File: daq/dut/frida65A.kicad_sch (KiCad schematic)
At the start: 65 parts, among them J1 SMA Molex 733910070, J2 SMA Molex 733910070, J3 RJ45 Molex 446200002, J4 DisplayPort Molex 472720024, J5 MiniFitJr Molex 469990014, J6 Conn_02x06_Top_Bottom, U1 ASIC FRIDA 65A, U2 LevelShifter TI TXV0106Q1, U3 DiffAmp TI THS4541

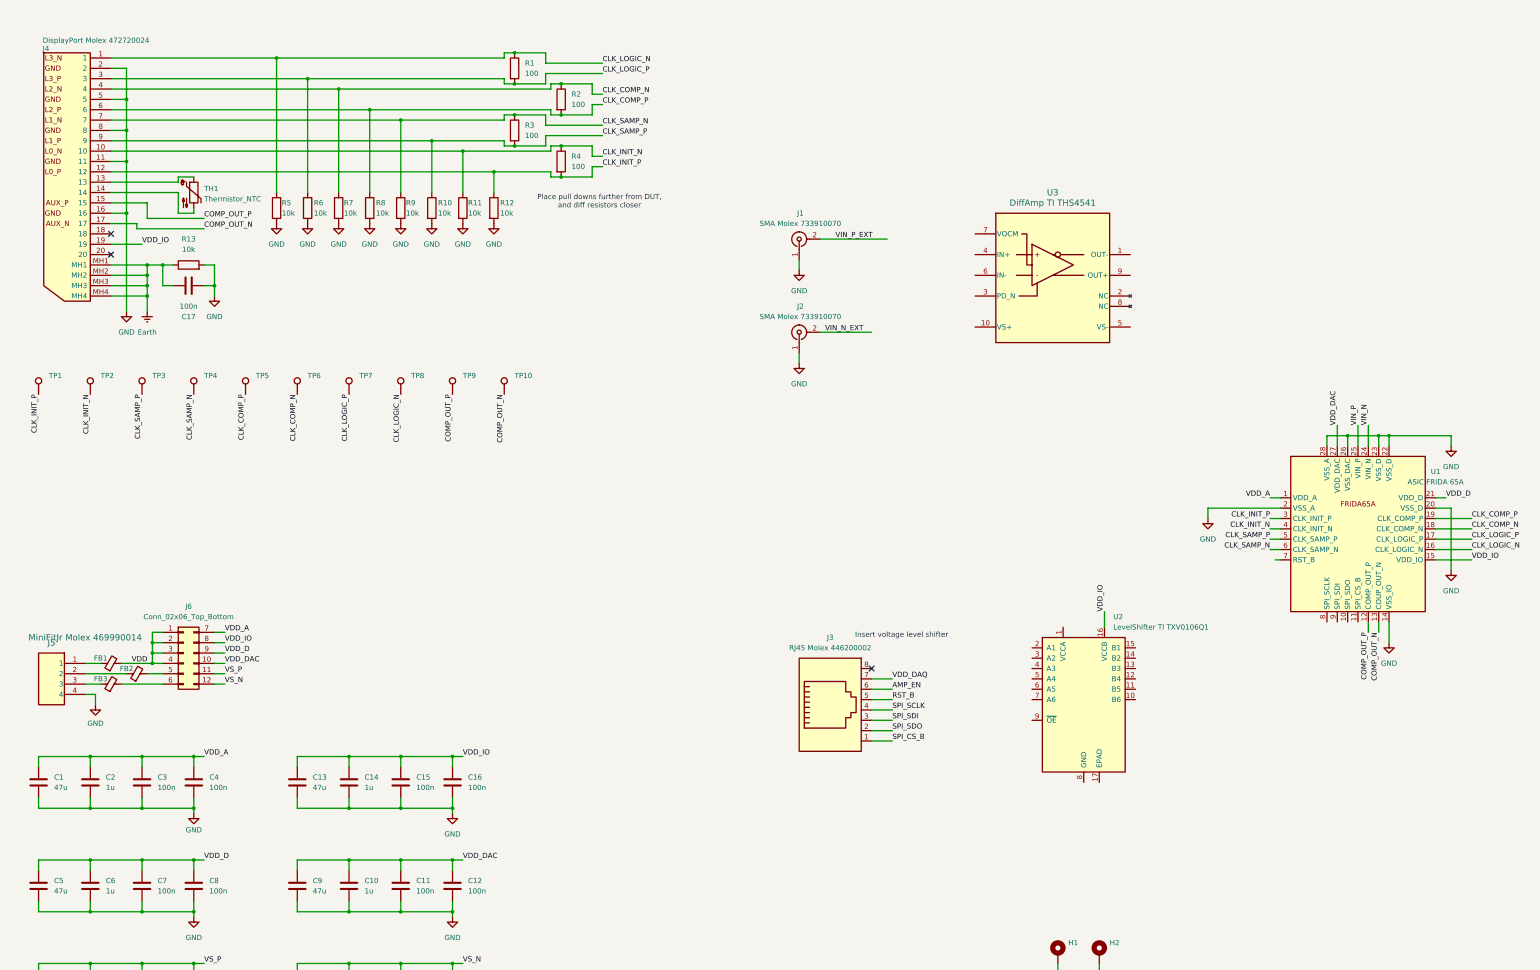
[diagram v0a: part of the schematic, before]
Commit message: Add connections for level shifter
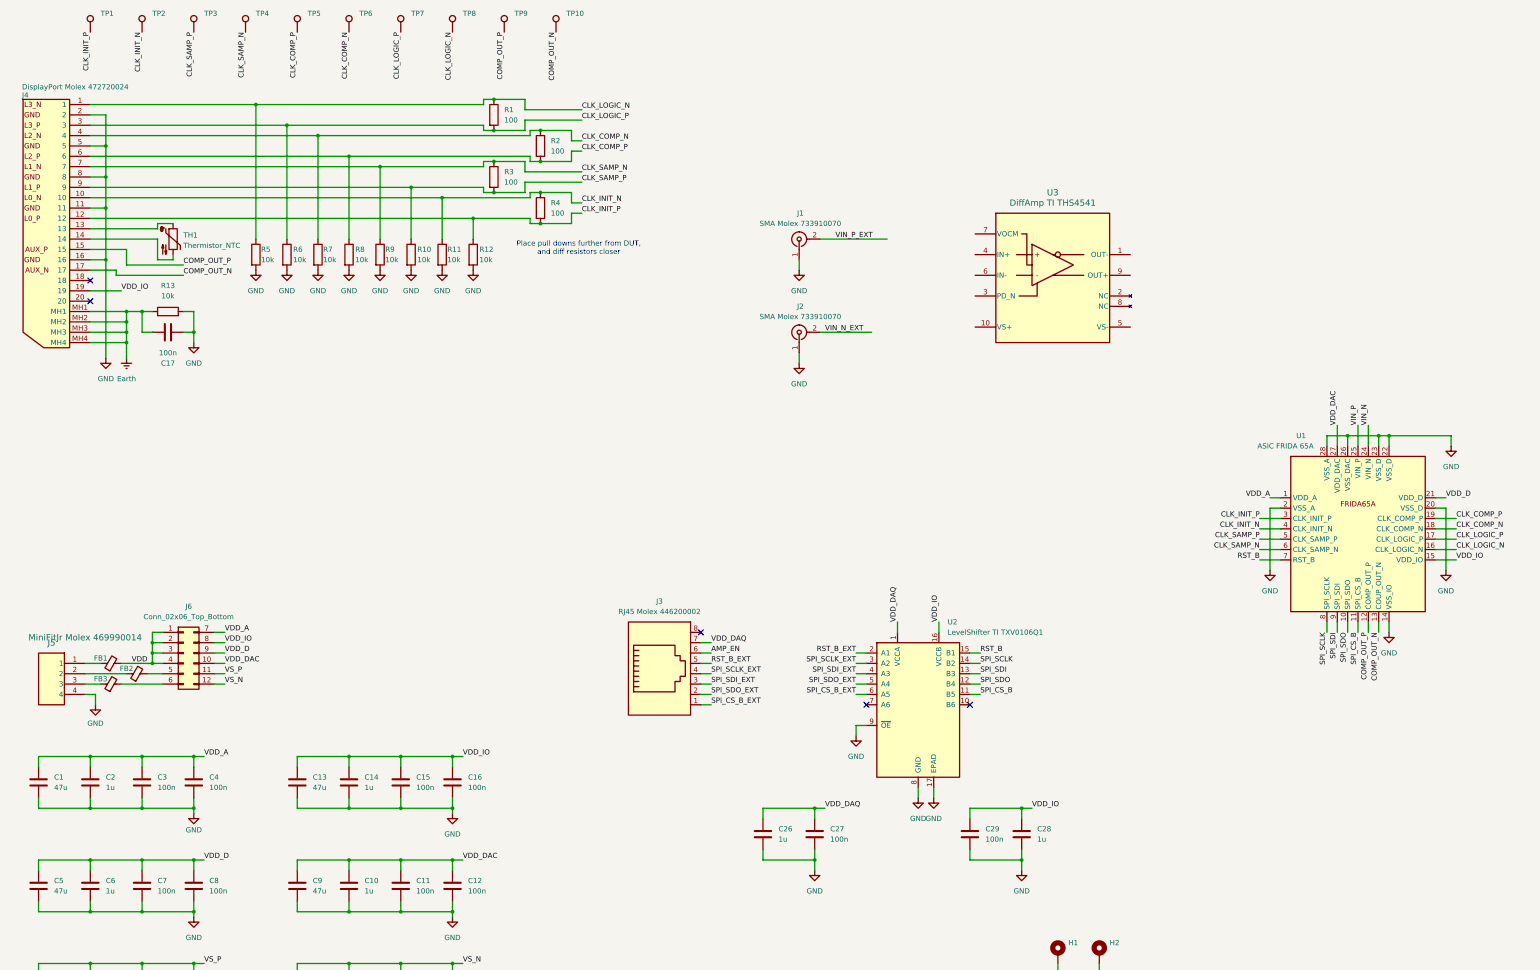
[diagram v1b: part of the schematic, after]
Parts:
- added C26, C28: 1u, Capacitor_SMD:C_0603_1608Metric, symbol Device:C
- added C27, C29: 100n, Capacitor_SMD:C_0603_1608Metric, symbol Device:C
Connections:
- net GND: now also U2.17 (EPAD), U2.8 (GND), U2.9 (~{OE}), C26.2, C27.2, C28.2, C29.2
- net RST_B: now also U1.7 (RST_B), U2.15 (B1); no longer J3.5
- net SPI_CS_B: now also U1.11 (SPI_CS_B), U2.11 (B5); no longer J3.1
- net SPI_SCLK: now also U1.8 (SPI_SCLK), U2.14 (B2); no longer J3.4
- net SPI_SDI: now also U1.9 (SPI_SDI), U2.13 (B3); no longer J3.3
- net SPI_SDO: now also U1.10 (SPI_SDO), U2.12 (B4); no longer J3.2
- net VDD_DAQ: now also U2.1 (VCCA), C26.1, C27.1
- net VDD_IO: now also C28.1, C29.1
- net RST_B_EXT: now reaches U2.2 (A1)
- net RST_B_EXT: now also J3.5
- net SPI_SCLK_EXT: now reaches U2.3 (A2)
- net SPI_SCLK_EXT: now also J3.4
- net SPI_SDI_EXT: now reaches U2.4 (A3)
- net SPI_SDI_EXT: now also J3.3
- net SPI_SDO_EXT: now reaches U2.5 (A4)
- net SPI_SDO_EXT: now also J3.2
- net SPI_CS_B_EXT: now reaches U2.6 (A5)
- net SPI_CS_B_EXT: now also J3.1
- no-connect marks 3 -> 5
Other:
- note removed: "Insert voltage level shifter"
- moved on the sheet: C17, J3, J4, R1, R10, R11, R12, R13, R2, R3, R4, R5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

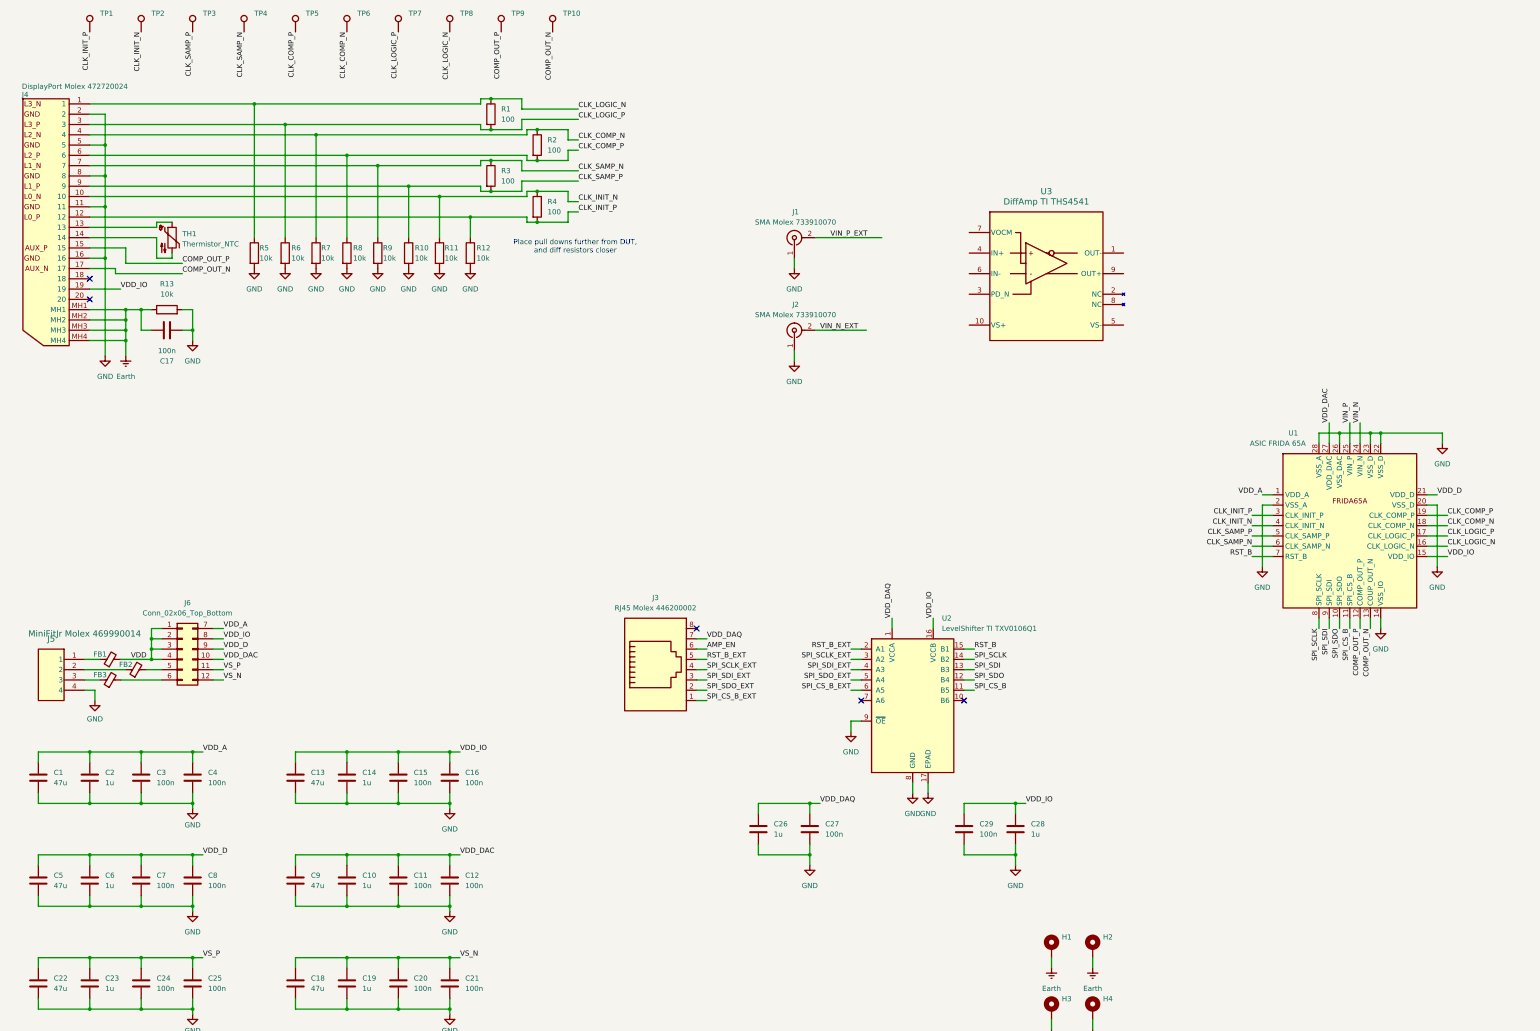
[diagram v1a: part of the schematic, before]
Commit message: Update PCB schematic, and differential layout traces
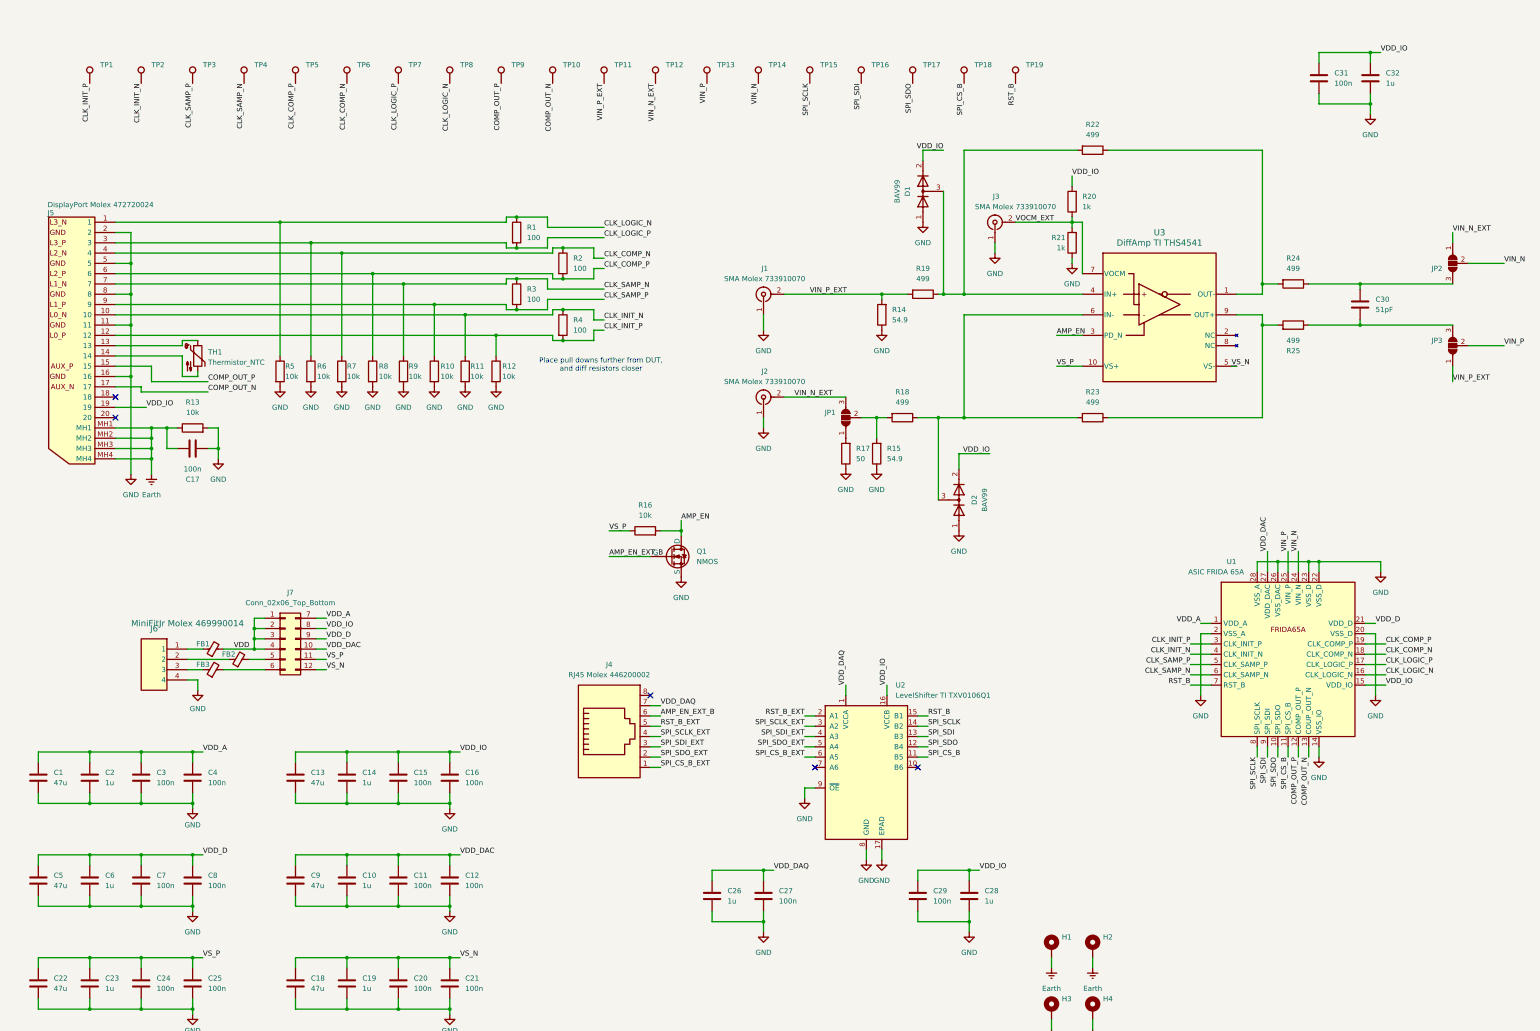
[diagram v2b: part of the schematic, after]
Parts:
- added C30: 51pF, Capacitor_SMD:C_0603_1608Metric, symbol Device:C
- added C31: 100n, Capacitor_SMD:C_0603_1608Metric, symbol Device:C
- added C32: 1u, Capacitor_SMD:C_0603_1608Metric, symbol Device:C
- added D1, D2: BAV99, Package_TO_SOT_SMD:SOT-23, symbol Diode:BAV99
- added J3: SMA Molex 733910070, frida:Molex_SMA_733910070, symbol frida:Molex_SMA_733910070
- added JP1, JP2, JP3: SolderJumper_3_Open, Jumper:SolderJumper-3_P1.3mm_Open_RoundedPad1.0x1.5mm_NumberLabels, symbol Jumper:SolderJumper_3_Open
- added Q1: NMOS, Package_TO_SOT_SMD:SOT-23, symbol Simulation_SPICE:NMOS
- added R14, R15: 54.9, Resistor_SMD:R_0603_1608Metric, symbol Device:R
- added R16: 10k, Resistor_SMD:R_0603_1608Metric, symbol Device:R
- added R17: 50, Resistor_SMD:R_0603_1608Metric, symbol Device:R
- added R18, R19, R22, R23, R24, R25: 499, Resistor_SMD:R_0603_1608Metric, symbol Device:R
- added R20, R21: 1k, Resistor_SMD:R_0603_1608Metric, symbol Device:R
- added TP11, TP12, TP13, TP14, TP15, TP16, TP17, TP18, TP19: TestPoint, TestPoint:TestPoint_Pad_D2.0mm, symbol Connector:TestPoint
- J7: renamed from J6; footprint (none) -> Connector_PinHeader_2.54mm:PinHeader_2x06_P2.54mm_Vertical
- TP1, TP10, TP2, TP3, TP4, TP5, TP6, TP7, TP8, TP9: footprint TestPoint:TestPoint_Keystone_5000-5004_Miniature -> frida:Test_Point
- renumbered J3 to J4, J4 to J5, J5 to J6
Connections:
- net AMP_EN: now also U3.3 (PD_N), Q1.1 (D), R16.2; no longer J4.6
- net GND: now also C31.2, C32.2, D1.1 (K), D2.1 (K), J3.1 (In), Q1.3 (S), R14.1, R15.1, R17.1, R21.1
- net RST_B: now also TP19.1
- net SPI_CS_B: now also TP18.1
- net SPI_SCLK: now also TP15.1
- net SPI_SDI: now also TP16.1
- net SPI_SDO: now also TP17.1
- net VDD_IO: now also C31.1, C32.1, D1.2 (A), D2.2 (A), R20.2
- net VIN_N: now also JP2.2 (C), TP14.1
- net VIN_N_EXT: now also JP1.3 (B), JP2.1 (A), TP12.1
- net VIN_P: now also JP3.2 (C), TP13.1
- net VIN_P_EXT: now also JP3.1 (A), R14.2, R19.2, TP11.1
- net VS_N: now also U3.5 (VS-)
- net VS_P: now also U3.10 (VS+), R16.1
- net at U3.1 (OUT-): now also R22.1, R24.2
- net at U3.4 (IN+): now also D1.3 (K), R19.1, R22.2
- net at U3.6 (IN-): now also D2.3 (K), R18.1, R23.2
- net VOCM_EXT: now reaches U3.7 (VOCM)
- net VOCM_EXT: now also J3.2 (Ext), R20.1, R21.2
- net at U3.9 (OUT+): now also R23.1, R25.2
- new net: JP1.2 (C), R15.2, R18.2
- new net: JP1.1 (A), R17.2
- new net: C30.1, JP2.3 (B), R24.1
- new net: C30.2, JP3.3 (B), R25.1
- new net AMP_EN_EXT_B: J4.6, Q1.2 (G)
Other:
- moved on the sheet: C17, C26, C27, C28, C29, FB1, FB2, FB3, J1, J2, J4, J5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

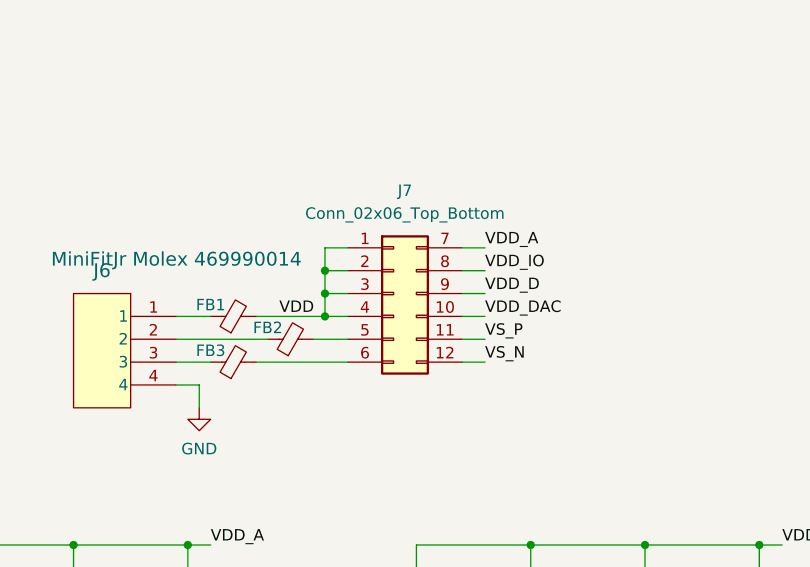
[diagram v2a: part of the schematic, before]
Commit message: Remove solder mask from footprints
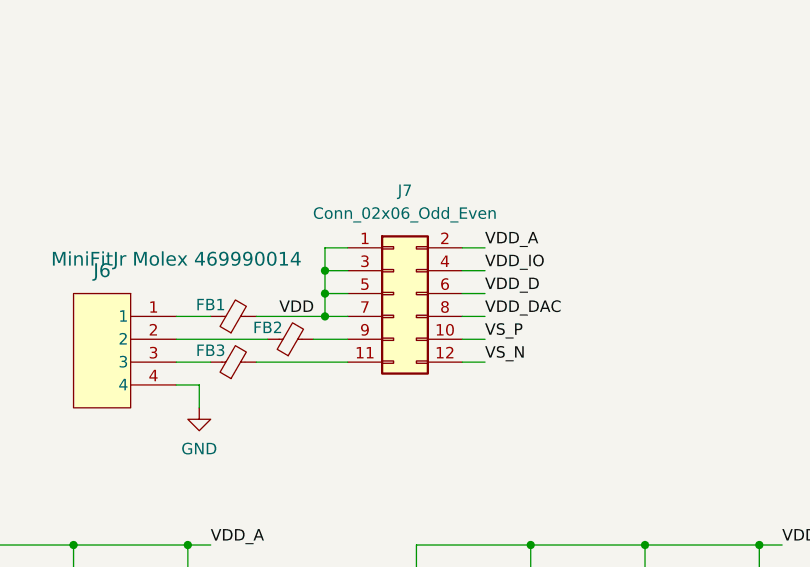
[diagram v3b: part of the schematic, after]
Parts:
- removed J7: Conn_02x06_Top_Bottom, Connector_PinHeader_2.54mm:PinHeader_2x06_P2.54mm_Vertical, symbol Connector_Generic:Conn_02x06_Top_Bottom
- added J7: Conn_02x06_Odd_Even, Connector_PinHeader_2.54mm:PinHeader_2x06_P2.54mm_Vertical, symbol Connector_Generic:Conn_02x06_Odd_Even
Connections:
- net VDD: now also J7.1 (Pin_1), J7.3 (Pin_3), J7.5 (Pin_5), J7.7 (Pin_7)
- net VDD_A: now also J7.2 (Pin_2)
- net VDD_D: now also J7.6 (Pin_6)
- net VDD_DAC: now also J7.8 (Pin_8)
- net VDD_IO: now also J7.4 (Pin_4)
- net VS_N: now also J7.12 (Pin_12)
- net VS_P: now also J7.10 (Pin_10)
- net at FB3.2: now also J7.11 (Pin_11)
- net at FB2.2: now also J7.9 (Pin_9)
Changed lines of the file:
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@@
+	)
+	(symbol
+		(lib_id "Connector_Generic:Conn_02x06_Odd_Even")
+		(at 86.36 175.26 0)
+		(unit 1)
+		(exclude_from_sim no)
+		(in_bom yes)
+		(on_board yes)
+		(dnp no)
+		(fields_autoplaced yes)
+		(property "Reference" "J7"
+			(at 87.63 163.83 0)
+			(effects
+				(font
+					(size 1.27 1.27)
+				)
+			)
+		)
+		(property "Value" "Conn_02x06_Odd_Even"
+			(at 87.63 166.37 0)
+			(effects
+				(font
+					(size 1.27 1.27)
+				)
+			)
+		)
+		(property "Footprint" "Connector_PinHeader_2.54mm:PinHeader_2x06_P2.54mm_Vertical"
+			(at 86.36 175.26 0)
+			(effects
+				(font
+					(size 1.27 1.27)
+				)
+				(hide yes)
+			)
+		)
+		(property "Datasheet" "~"
+			(at 86.36 175.26 0)
+			(effects
+				(font
+					(size 1.27 1.27)
+				)
+				(hide yes)
+			)
+		)
+		(property "Description" "Generic connector, double row, 02x06, odd/even pin numbering scheme (row 1 odd numbers, row 2 even numbers), script generated (kicad-library-utils/schlib/autogen/connector/)"
+			(at 86.36 175.26 0)
+			(effects
+				(font
+					(size 1.27 1.27)
+				)
+				(hide yes)
+			)
+		)
+		(pin "8"
+		)
+		(pin "4"
+		)
+		(pin "3"
+		)
+		(pin "9"
+		)
+		(pin "11"
+		)
+		(pin "2"
+		)
+		(pin "10"
+		)
+		(pin "1"
+		)
+		(pin "12"
+		)
+		(pin "5"
+		)
+		(pin "7"
+		)
+		(pin "6"
+		)
+		(instances
+			(project ""
+				(path "/fa3d0b93-951b-4460-b2d5-04f3ffae1154"
+					(reference "J7")
+					(unit 1)
+				)
+			)
+		)
 	)
 	(symbol
@@
 					(unit 1)
 				)
-			)
-		)
-	)
-	(symbol
-		(lib_id "Connector_Generic:Conn_02x06_Top_Bottom")
-		(at 86.36 175.26 0)
-		(unit 1)
-		(exclude_from_sim no)
-		(in_bom yes)
-		(on_board yes)
-		(dnp no)
-		(fields_autoplaced yes)
-		(property "Reference" "J7"
-			(at 87.63 163.83 0)
-			(effects
-				(font
-					(size 1.27 1.27)
-				)
-			)
-		)
-		(property "Value" "Conn_02x06_Top_Bottom"
-			(at 87.63 166.37 0)
-			(effects
-				(font
-					(size 1.27 1.27)
-				)
-			)
-		)
-		(property "Footprint" "Connector_PinHeader_2.54mm:PinHeader_2x06_P2.54mm_Vertical"
-			(at 86.36 175.26 0)
-			(effects
-				(font
-					(size 1.27 1.27)
-				)
-				(hide yes)
-			)
-		)
-		(property "Datasheet" "~"
-			(at 86.36 175.26 0)
-			(effects
-				(font
-					(size 1.27 1.27)
-				)
-				(hide yes)
-			)
-		)
-		(property "Description" "Generic connector, double row, 02x06, top/bottom pin numbering scheme (row 1: 1...pins_per_row, row2: pins_per_row+1 ... num_pins), script generated (kicad-library-utils/schlib/autogen/connector/)"
-			(at 86.36 175.26 0)
-			(effects
-				(font
-					(size 1.27 1.27)
-				)
-				(hide yes)
-			)
-		)
-		(pin "4"
-		)
-		(pin "5"
-		)
-		(pin "8"
-		)
-		(pin "3"
-		)
-		(pin "1"
-		)
-		(pin "6"
-		)
-		(pin "12"
-		)
-		(pin "11"
-		)
-		(pin "10"
-		)
-		(pin "2"
-		)
-		(pin "9"
-		)
-		(pin "7"
-		)
-		(instances
-			(project ""
-				(path "/fa3d0b93-951b-4460-b2d5-04f3ffae1154"
-					(reference "J7")
-					(unit 1)
-				)
